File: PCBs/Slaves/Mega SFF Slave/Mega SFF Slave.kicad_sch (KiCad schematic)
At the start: 79 parts, among them J1 AVR-ISP-6, J10 Screw_Terminal_01x02, J11 Screw_Terminal_01x02, J12 Screw_Terminal_01x02, J13 Screw_Terminal_01x02, J14 Screw_Terminal_01x02, J15 Screw_Terminal_01x02, J16 Screw_Terminal_01x02, J17 Screw_Terminal_01x02, J18 Screw_Terminal_01x02, J19 Screw_Terminal_01x02, J2 Screw_Terminal_01x02, J20 Screw_Terminal_01x02, J21 Screw_Terminal_01x02, J22 Screw_Terminal_01x02, J23 Screw_Terminal_01x02, J24 Screw_Terminal_01x02, J25 Screw_Terminal_01x02, J26 Screw_Terminal_01x02, J27 Screw_Terminal_01x02, J28 Screw_Terminal_01x02, J29 Screw_Terminal_01x02, J3 Screw_Terminal_01x02, J30 Screw_Terminal_01x02, J31 Screw_Terminal_01x02, J32 Screw_Terminal_01x02, J33 Screw_Terminal_01x02, J34 Screw_Terminal_01x02, J35 Screw_Terminal_01x02, J36 Screw_Terminal_01x02, J37 Screw_Terminal_01x02, J39 Conn_01x06_Female, J4 Screw_Terminal_01x02, J40 Screw_Terminal_01x02, J41 Screw_Terminal_01x02, J5 Screw_Terminal_01x02, J6 Screw_Terminal_01x02, J7 Screw_Terminal_01x02, J8 Screw_Terminal_01x02, J9 Screw_Terminal_01x02, SW1 SW_MEC_5E, SW2 SW_DIP_x02, SW3 SW_DIP_x02, U1 ATmega2560-16A, U2 MAX487ESA+T, U3 AMS1117-5.0, U4 ULN2003A, U5 MAX487ESA+T, Y1 Crystal_GND24

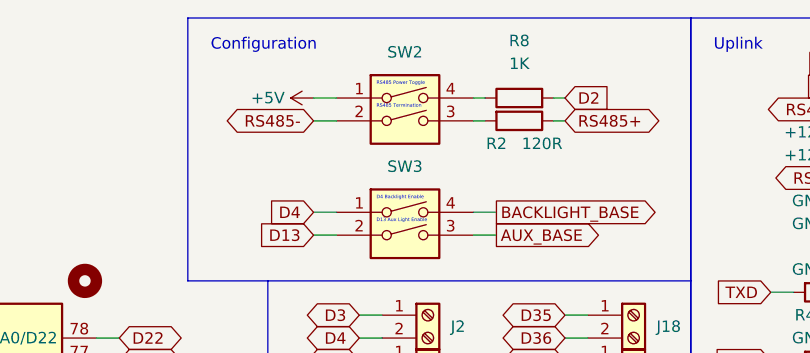
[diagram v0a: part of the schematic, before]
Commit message: Updated Mega SFF Slave RS485 Switch and Silkscreen
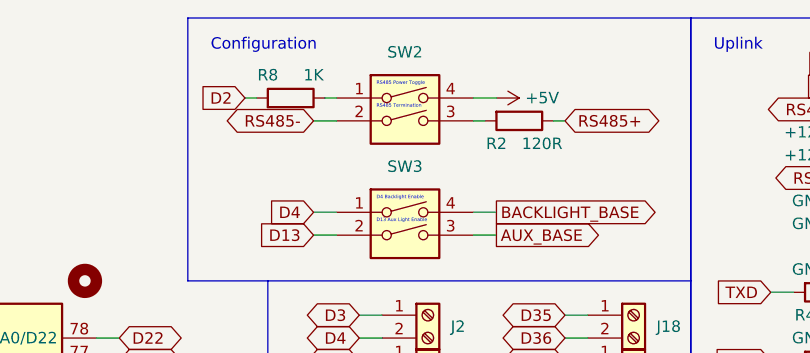
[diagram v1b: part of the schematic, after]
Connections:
- net +5V: now also SW2.4; no longer SW2.1
- net at R8.1: now also SW2.1; no longer SW2.4
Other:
- moved on the sheet: R8
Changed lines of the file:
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@@
     (stroke (width 0) (type default) (color 0 0 0 0))
   )
-  (wire (pts (xy 209.55 21.59) (xy 210.82 21.59))
+  (wire (pts (xy 194.31 21.59) (xy 193.04 21.59))
     (stroke (width 0) (type default) (color 0 0 0 0))
   )
@@
     (stroke (width 0) (type default) (color 0 0 0 0))
   )
-  (wire (pts (xy 219.71 21.59) (xy 218.44 21.59))
+  (wire (pts (xy 184.15 21.59) (xy 185.42 21.59))
     (stroke (width 0) (type default) (color 0 0 0 0))
   )
@@
     (stroke (width 0) (type default) (color 0 0 0 0))
   )
-  (wire (pts (xy 191.77 21.59) (xy 194.31 21.59))
+  (wire (pts (xy 212.09 21.59) (xy 209.55 21.59))
     (stroke (width 0) (type default) (color 0 0 0 0))
   )
@@
     )
   )
-  (global_label "D2" (shape input) (at 219.71 21.59 0) (fields_autoplaced)
-    (effects (font (size 1.27 1.27)) (justify left))
-    (property "Intersheet References" "${INTERSHEET_REFS}" (id 0) (at 224.6026 21.5106 0)
-      (effects (font (size 1.27 1.27)) (justify left) hide)
+  (global_label "D2" (shape input) (at 184.15 21.59 180) (fields_autoplaced)
+    (effects (font (size 1.27 1.27)) (justify right))
+    (property "Intersheet References" "${INTERSHEET_REFS}" (id 0) (at 179.2574 21.5106 0)
+      (effects (font (size 1.27 1.27)) (justify right) hide)
     )
   )
@@
     (pin "2")
   )
-  (symbol (lib_id "Device:R") (at 214.63 21.59 90) (unit 1)
-    (in_bom yes) (on_board yes) (fields_autoplaced)
-    (property "Reference" "R8" (id 0) (at 214.63 15.24 90))
-    (property "Value" "1K" (id 1) (at 214.63 17.78 90))
-    (property "Footprint" "Resistor_SMD:R_0805_2012Metric" (id 2) (at 214.63 23.368 90)
-      (effects (font (size 1.27 1.27)) hide)
-    )
-    (property "Datasheet" "~" (id 3) (at 214.63 21.59 0)
-      (effects (font (size 1.27 1.27)) hide)
-    )
-    (property "LCSC" "C17513" (id 4) (at 214.63 21.59 0)
+  (symbol (lib_id "Device:R") (at 189.23 21.59 270) (mirror x) (unit 1)
+    (in_bom yes) (on_board yes)
+    (property "Reference" "R8" (id 0) (at 186.69 19.05 90))
+    (property "Value" "1K" (id 1) (at 191.77 19.05 90))
+    (property "Footprint" "Resistor_SMD:R_0805_2012Metric" (id 2) (at 189.23 23.368 90)
+      (effects (font (size 1.27 1.27)) hide)
+    )
+    (property "Datasheet" "~" (id 3) (at 189.23 21.59 0)
+      (effects (font (size 1.27 1.27)) hide)
+    )
+    (property "LCSC" "C17513" (id 4) (at 189.23 21.59 0)
       (effects (font (size 1.27 1.27)) hide)
     )
@@
     (pin "2")
   )
-  (symbol (lib_id "power:+5V") (at 191.77 21.59 90) (unit 1)
+  (symbol (lib_id "power:+5V") (at 212.09 21.59 270) (mirror x) (unit 1)
     (in_bom yes) (on_board yes)
-    (property "Reference" "#PWR03" (id 0) (at 195.58 21.59 0)
-      (effects (font (size 1.27 1.27)) hide)
-    )
-    (property "Value" "+5V" (id 1) (at 186.69 21.59 90))
-    (property "Footprint" "" (id 2) (at 191.77 21.59 0)
-      (effects (font (size 1.27 1.27)) hide)
-    )
-    (property "Datasheet" "" (id 3) (at 191.77 21.59 0)
-      (effects (font (size 1.27 1.27)) hide)
-    )
+    (property "Reference" "#PWR03" (id 0) (at 208.28 21.59 0)
+      (effects (font (size 1.27 1.27)) hide)
+    )
+    (property "Value" "+5V" (id 1) (at 217.17 21.59 90))
+    (property "Footprint" "" (id 2) (at 212.09 21.59 0)
+      (effects (font (size 1.27 1.27)) hide)
+    )
+    (property "Datasheet" "" (id 3) (at 212.09 21.59 0)
+      (effects (font (size 1.27 1.27)) hide)
+    )

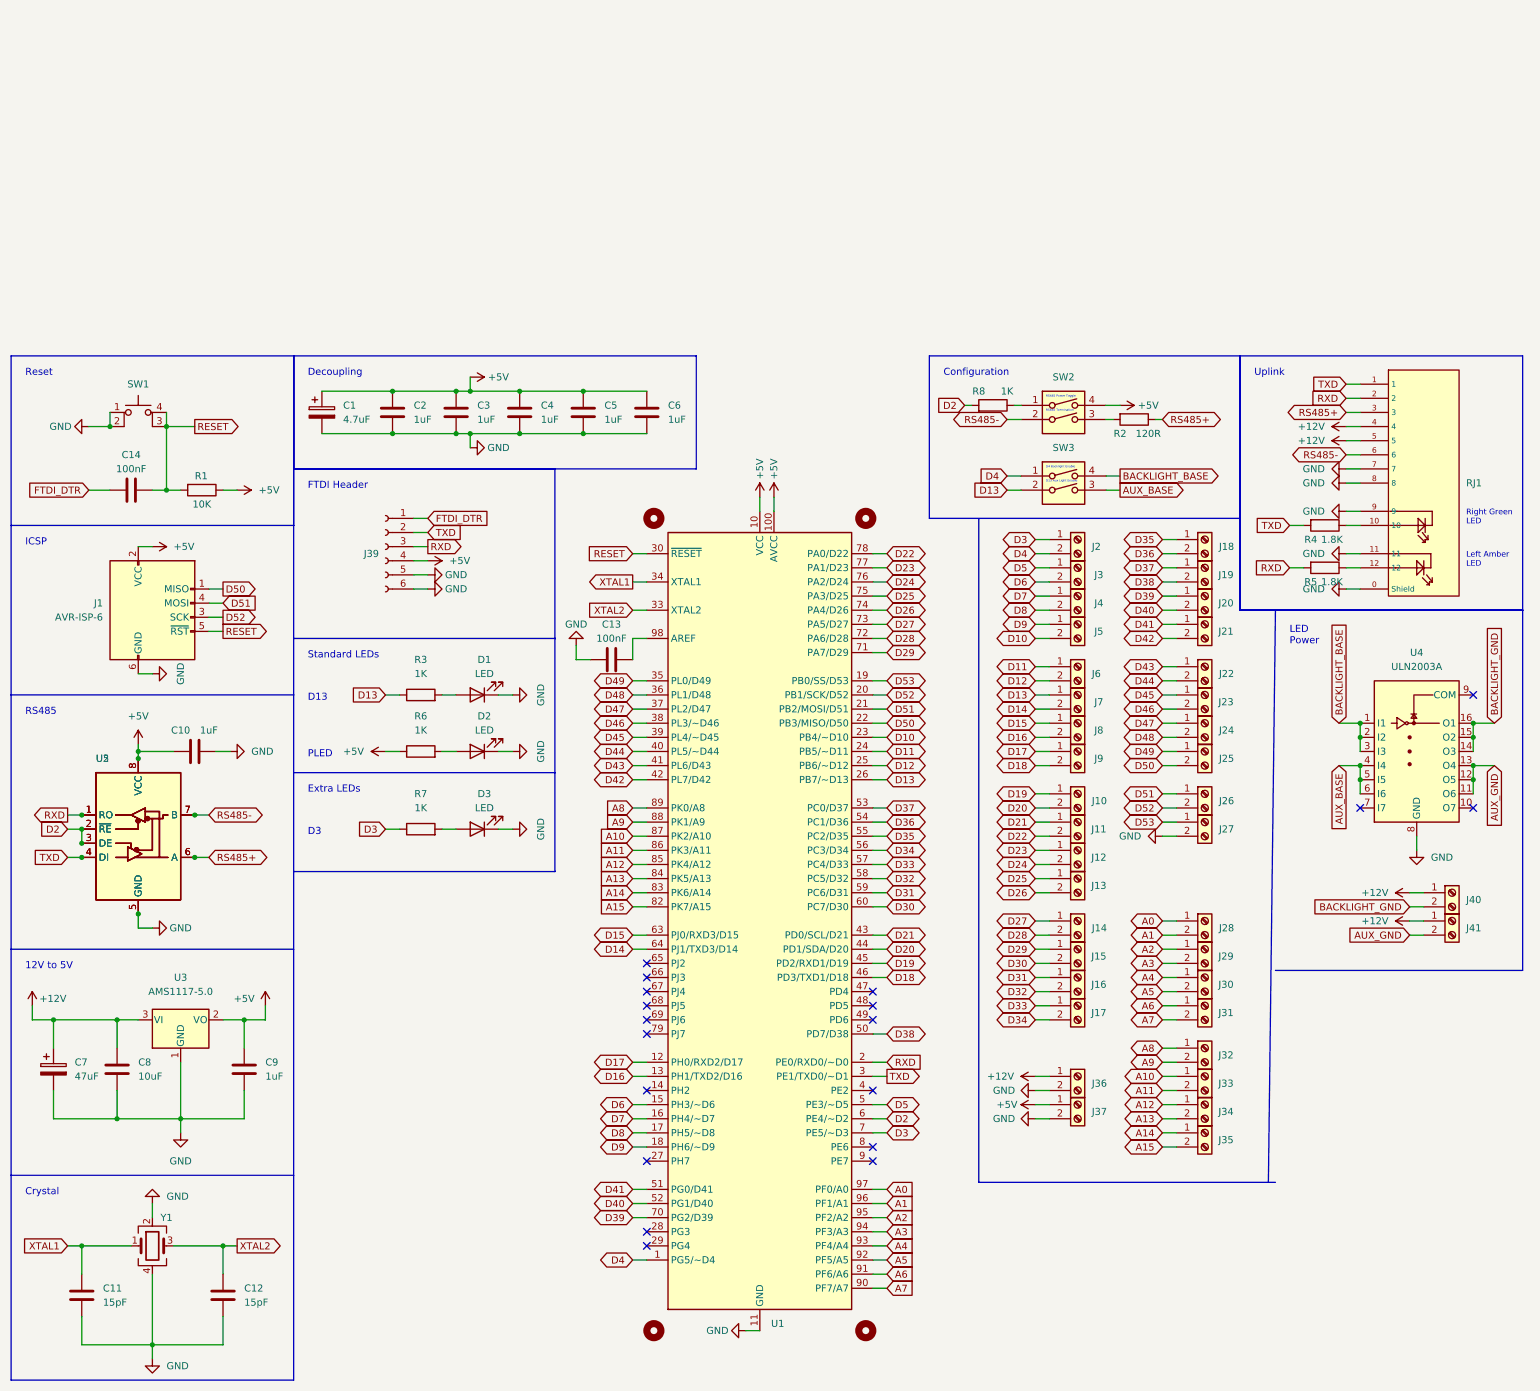
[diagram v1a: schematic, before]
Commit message: Added Hotplug and RS485 protection to Mega SFF Schematic. PCB to go
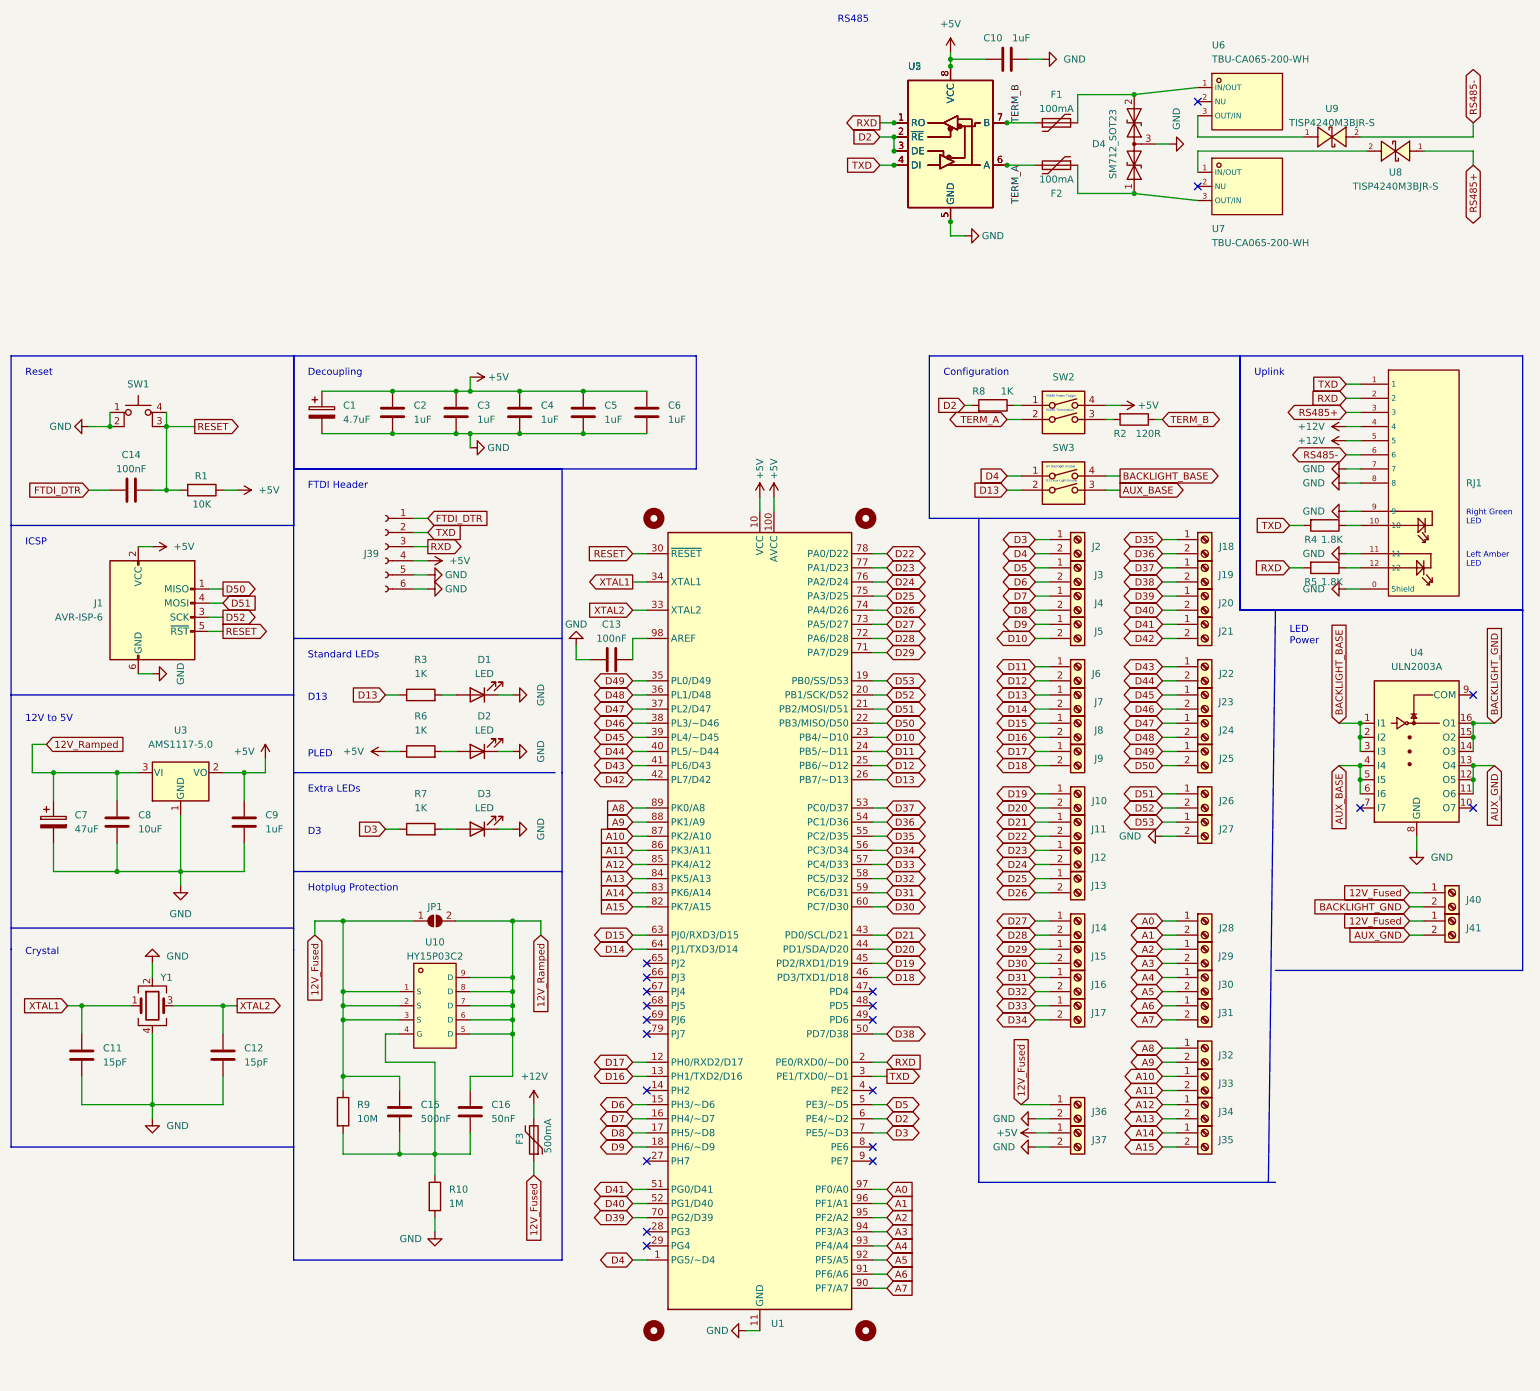
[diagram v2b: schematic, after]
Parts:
- added C15: 500nF, A10 KiCad Libraries:C0402, symbol Device:C
- added C16: 50nF, A10 KiCad Libraries:C0402, symbol Device:C
- added D4: SM712_SOT23, Package_TO_SOT_SMD:SOT-23, symbol Diode:SM712_SOT23
- added F1, F2: 100mA, Fuse:Fuse_0603_1608Metric, symbol Device:Polyfuse
- added F3: 500mA, Fuse:Fuse_1206_3216Metric, symbol Device:Polyfuse
- added JP1: Solder, Jumper:SolderJumper-2_P1.3mm_Open_RoundedPad1.0x1.5mm, symbol Jumper:SolderJumper_2_Open
- added R10: 1M, Resistor_SMD:R_0603_1608Metric, symbol Device:R
- added R9: 10M, Resistor_SMD:R_0603_1608Metric, symbol Device:R
- added U10: HY15P03C2, A10 KiCad Libraries:DFN-8_L5.9-W5.2-P1.27-LS6.2-BL, symbol A10:HY15P03C2
- added U6, U7: TBU-CA065-200-WH, A10 KiCad Libraries:DIO-SMD_3P-L6.5-W4.0-BI, symbol A10:TBU-CA065-200-WH
- added U8, U9: TISP4240M3BJR-S, A10 KiCad Libraries:DO-214AA_L4.4-W3.6-LS5.3-BI, symbol A10:TISP4240M3BJR-S
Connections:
- net +12V: now also F3.2; no longer C7.1, C8.1, J36.1 (Pin_1), J40.1 (Pin_1), J41.1 (Pin_1), U3.3 (VI)
- net GND: now also D4.3 (common), R10.2
- net RS485+: now also U8.1 (A); no longer R2.1, U2.6 (A), U5.6 (A)
- net RS485-: now also U9.2 (K); no longer SW2.2, U2.7 (B), U5.7 (B)
- new net: D4.1 (A1), F2.1, U7.3 (OUT/IN)
- new net: D4.2 (A2), F1.2, U6.1 (IN/OUT)
- new net: C15.2, C16.2, R10.1, R9.2, U10.4 (G)
- new net: U7.1 (IN/OUT), U8.2 (K)
- new net: U6.3 (OUT/IN), U9.1 (A)
- new net 12V_Fused: C15.1, F3.1, J36.1 (Pin_1), J40.1 (Pin_1), J41.1 (Pin_1), JP1.1 (A), R9.1, U10.1 (S), U10.2 (S), U10.3 (S)
- new net 12V_Ramped: C16.1, C7.1, C8.1, JP1.2 (B), U10.5 (D), U10.6 (D), U10.7 (D), U10.8 (D), U10.9 (D), U3.3 (VI)
- new net TERM_A: F2.2, SW2.2, U2.6 (A), U5.6 (A)
- new net TERM_B: F1.1, R2.1, U2.7 (B), U5.7 (B)
- no-connect marks 19 -> 21
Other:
- note added: "Hotplug Protection"
- moved on the sheet: C10, C11, C12, C7, C8, C9, J36, J37, U2, U3, U5, Y1

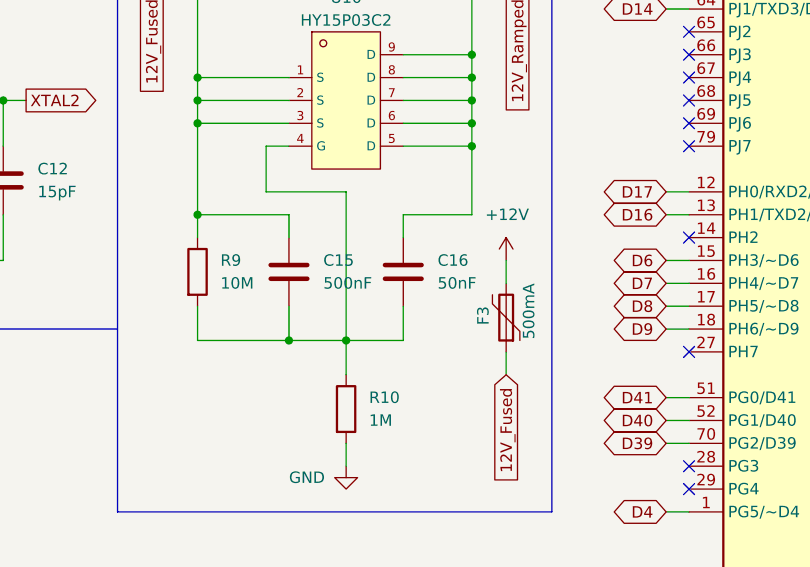
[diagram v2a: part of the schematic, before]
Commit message: Updated LCSC number and size of voltage ramp capacitors for Mega SFF Slave
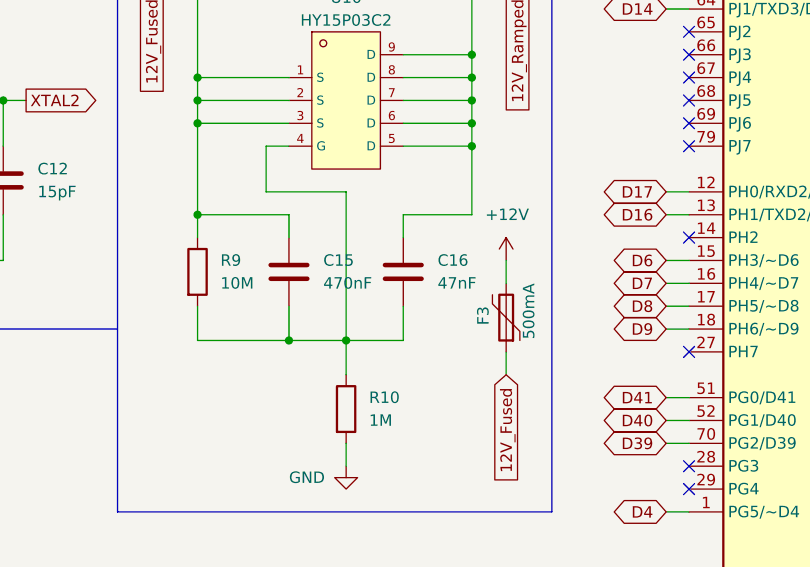
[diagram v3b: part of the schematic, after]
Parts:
- C15: value 500nF -> 470nF; footprint A10 KiCad Libraries:C0402 -> Capacitor_SMD:C_0603_1608Metric; LCSC TBA -> C1623
- C16: value 50nF -> 47nF; footprint A10 KiCad Libraries:C0402 -> Capacitor_SMD:C_0603_1608Metric; LCSC TBA -> C1622
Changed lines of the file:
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@@
       (effects (font (size 1.27 1.27)) (justify left))
     )
-    (property "Value" "500nF" (id 1) (at 86.36 149.8599 0)
-      (effects (font (size 1.27 1.27)) (justify left))
-    )
-    (property "Footprint" "A10 KiCad Libraries:C0402" (id 2) (at 83.5152 152.4 0)
+    (property "Value" "470nF" (id 1) (at 86.36 149.8599 0)
+      (effects (font (size 1.27 1.27)) (justify left))
+    )
+    (property "Footprint" "Capacitor_SMD:C_0603_1608Metric" (id 2) (at 83.5152 152.4 0)
       (effects (font (size 1.27 1.27)) hide)
     )
@@
       (effects (font (size 1.27 1.27)) hide)
     )
-    (property "LCSC" "TBA" (id 4) (at 82.55 148.59 0)
+    (property "LCSC" "C1623" (id 4) (at 82.55 148.59 0)
       (effects (font (size 1.27 1.27)) hide)
     )
@@
       (effects (font (size 1.27 1.27)) (justify left))
     )
-    (property "Value" "50nF" (id 1) (at 99.06 149.8599 0)
-      (effects (font (size 1.27 1.27)) (justify left))
-    )
-    (property "Footprint" "A10 KiCad Libraries:C0402" (id 2) (at 96.2152 152.4 0)
+    (property "Value" "47nF" (id 1) (at 99.06 149.8599 0)
+      (effects (font (size 1.27 1.27)) (justify left))
+    )
+    (property "Footprint" "Capacitor_SMD:C_0603_1608Metric" (id 2) (at 96.2152 152.4 0)
       (effects (font (size 1.27 1.27)) hide)
     )
@@
       (effects (font (size 1.27 1.27)) hide)
     )
-    (property "LCSC" "TBA" (id 4) (at 95.25 148.59 0)
+    (property "LCSC" "C1622" (id 4) (at 95.25 148.59 0)
       (effects (font (size 1.27 1.27)) hide)
     )
@@
     )
     (path "/2d6fb052-36d8-4f7b-b1d1-450a695be0f5"
-      (reference "C15") (unit 1) (value "500nF") (footprint "A10 KiCad Libraries:C0402")
+      (reference "C15") (unit 1) (value "470nF") (footprint "Capacitor_SMD:C_0603_1608Metric")
     )
     (path "/fc20ecea-8ca6-4141-a4ef-61c51fae915f"
-      (reference "C16") (unit 1) (value "50nF") (footprint "A10 KiCad Libraries:C0402")
+      (reference "C16") (unit 1) (value "47nF") (footprint "Capacitor_SMD:C_0603_1608Metric")
     )
     (path "/8cb5e783-a9af-473a-a8fd-77b6a468a9a2"
